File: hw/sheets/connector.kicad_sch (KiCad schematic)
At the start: 1 part, among them J1 AH58893-T9B10-3F

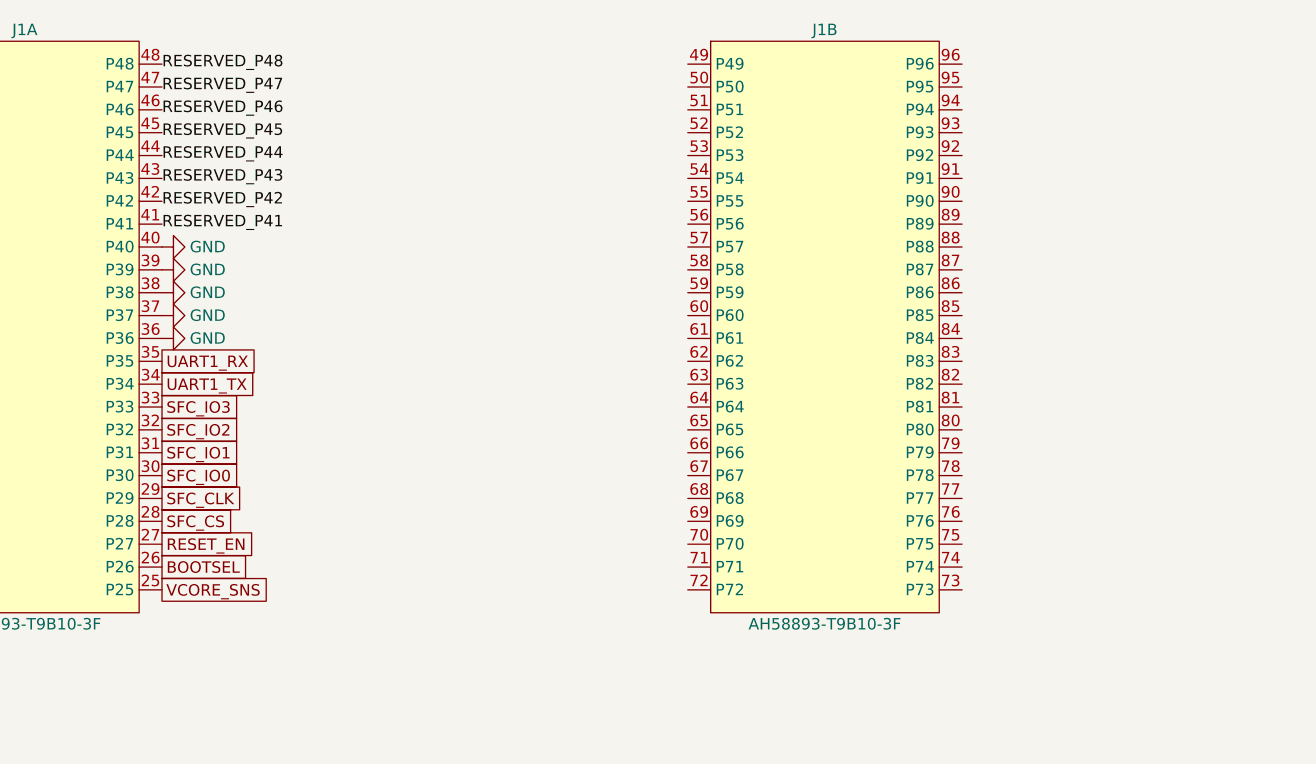
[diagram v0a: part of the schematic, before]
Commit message: Carrier board: BMC power isolation, ESP-Hosted link, GPIO expander
Rebuilds the schematic to connectivity-by-label per BUILD.md (zero
wires/junctions) across all four sections, and adds the BMC power
architecture, connector crossings, and safety fixes worked out this
session:

- Dedicated BMC USB-C (J9), isolated 5V domains (+5V_BMC/+5V_ALT/+5V_SW),
  priority DC-jack-over-USB-C P-FET OR (Q1/Q2), 2:1 load-switch select
  (U4/U14) with a genuine ON-OFF-ON manual override (SW2)
- D1/D2 diode-OR so the BMC stays powered on ALT-only input without
  reopening the J9 backfeed path
- JP1 provisioning jumper + mandatory bring-up checklist: gates SW2 until
  the digipot's NV memory has been confirmed safe, closing the
  factory-mid-scale-default overvoltage gap on VCORE
- GPIO expander (U15, TCA9555PWR) frees 9 ESP32 GPIOs for a full-duplex
  SPI link to the interposer SoC (ESP-Hosted WiFi/BLE co-processor),
  while keeping flash chip-select and power-domain switching native for
  margin testing
- microSD, headphone jack, and both MIPI camera FFCs now cross the DDR4
  connector to the interposer, with GND isolation around each block
- J2/J3 share one USB host data pair to the interposer (peripheral use,
  independent of J2's power role)
- Added missing primary SOIC-8 NOR flash chip (W25Q32JVSS) to match the
  reference board's dual-NOR layout

docs/UNIVERSAL.md updated throughout to match; CONNECTIONS.txt and the
ESP32 pinout reference regenerated from the current netlist.
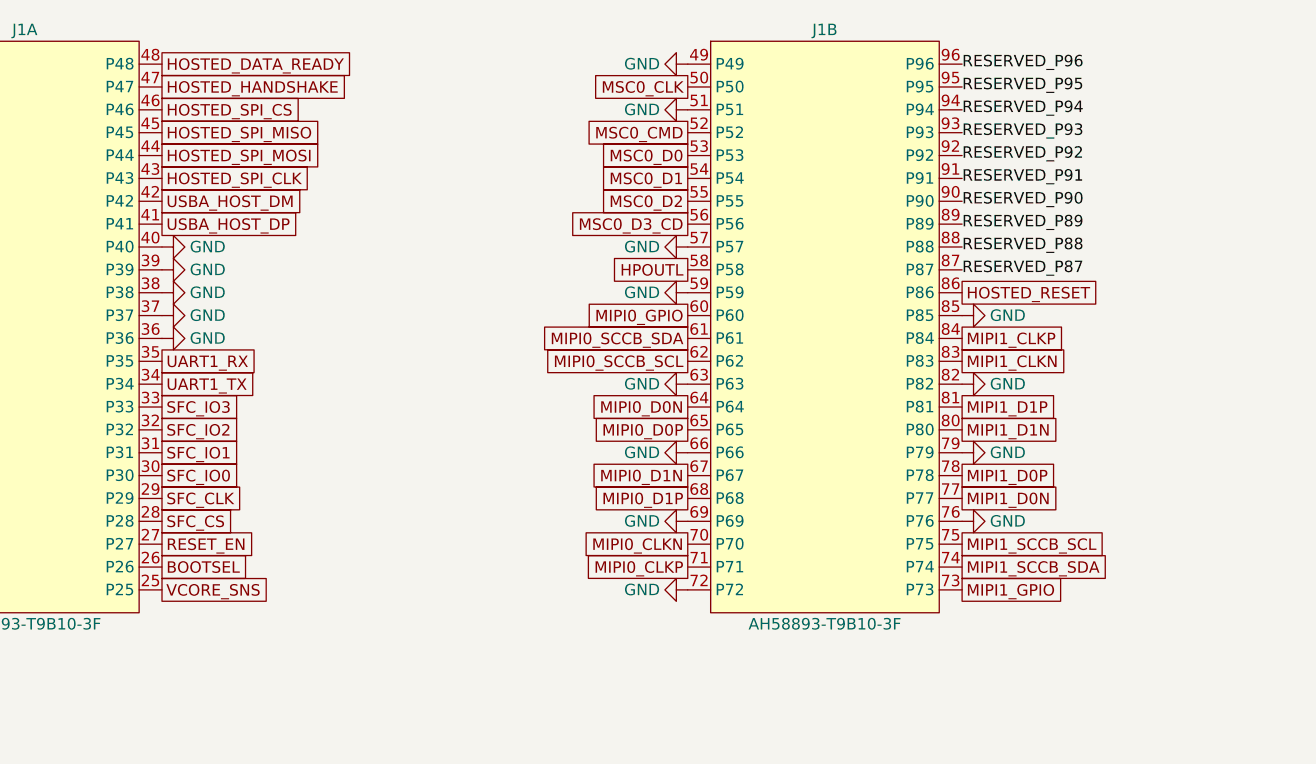
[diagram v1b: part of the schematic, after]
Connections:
- net GND: now also J1.49 (P49), J1.51 (P51), J1.57 (P57), J1.59 (P59), J1.63 (P63), J1.66 (P66), J1.69 (P69), J1.72 (P72), J1.76 (P76), J1.79 (P79), J1.82 (P82), J1.85 (P85)
- net MSC0_CLK: now reaches J1.50 (P50)
- net MSC0_CMD: now reaches J1.52 (P52)
- net MSC0_D0: now reaches J1.53 (P53)
- net MSC0_D1: now reaches J1.54 (P54)
- net MSC0_D2: now reaches J1.55 (P55)
- net MSC0_D3_CD: now reaches J1.56 (P56)
- net HPOUTL: now reaches J1.58 (P58)
- net MIPI0_GPIO: now reaches J1.60 (P60)
- net MIPI0_SCCB_SDA: now reaches J1.61 (P61)
- net MIPI0_SCCB_SCL: now reaches J1.62 (P62)
- net MIPI0_D0N: now reaches J1.64 (P64)
- net MIPI0_D0P: now reaches J1.65 (P65)
- net MIPI0_D1N: now reaches J1.67 (P67)
- net MIPI0_D1P: now reaches J1.68 (P68)
- net MIPI0_CLKN: now reaches J1.70 (P70)
- net MIPI0_CLKP: now reaches J1.71 (P71)
- net MIPI1_GPIO: now reaches J1.73 (P73)
- net MIPI1_SCCB_SDA: now reaches J1.74 (P74)
- net MIPI1_SCCB_SCL: now reaches J1.75 (P75)
- net MIPI1_D0N: now reaches J1.77 (P77)
- net MIPI1_D0P: now reaches J1.78 (P78)
- net MIPI1_D1N: now reaches J1.80 (P80)
- net MIPI1_D1P: now reaches J1.81 (P81)
- net MIPI1_CLKN: now reaches J1.83 (P83)
- net MIPI1_CLKP: now reaches J1.84 (P84)
- net HOSTED_RESET: now reaches J1.86 (P86)
- net RESERVED_P87: now reaches J1.87 (P87)
- net RESERVED_P88: now reaches J1.88 (P88)
- net RESERVED_P89: now reaches J1.89 (P89)
- net RESERVED_P90: now reaches J1.90 (P90)
- net RESERVED_P91: now reaches J1.91 (P91)
- net RESERVED_P92: now reaches J1.92 (P92)
- net RESERVED_P93: now reaches J1.93 (P93)
- net RESERVED_P94: now reaches J1.94 (P94)
- net RESERVED_P95: now reaches J1.95 (P95)
- net RESERVED_P96: now reaches J1.96 (P96)
- net RESERVED_P41 renamed USBA_HOST_DP
- net RESERVED_P42 renamed USBA_HOST_DM
- net RESERVED_P43 renamed HOSTED_SPI_CLK
- net RESERVED_P44 renamed HOSTED_SPI_MOSI
- net RESERVED_P45 renamed HOSTED_SPI_MISO
- net RESERVED_P46 renamed HOSTED_SPI_CS
- net RESERVED_P47 renamed HOSTED_HANDSHAKE
- net RESERVED_P48 renamed HOSTED_DATA_READY
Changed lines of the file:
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@@
 		(property "Value" "AH58893-T9B10-3F" (at 139.7 104.14000000000001 0) (effects (font (size 1.27 1.27))))
+	)
+	(symbol (lib_id "power:GND") (at 124.46 41.91 270) (unit 1)
+		(property "Reference" "#CGND016" (at 124.46 41.91 0) (effects (font (size 1.27 1.27)) hide))
+		(property "Value" "GND" (at 119.38 41.91 90) (effects (font (size 1.27 1.27))))
+	)
+	(symbol (lib_id "power:GND") (at 124.46 46.99 270) (unit 1)
+		(property "Reference" "#CGND017" (at 124.46 46.99 0) (effects (font (size 1.27 1.27)) hide))
+		(property "Value" "GND" (at 119.38 46.99 90) (effects (font (size 1.27 1.27))))
+	)
+	(symbol (lib_id "power:GND") (at 124.46 62.23 270) (unit 1)
+		(property "Reference" "#CGND018" (at 124.46 62.23 0) (effects (font (size 1.27 1.27)) hide))
+		(property "Value" "GND" (at 119.38 62.23 90) (effects (font (size 1.27 1.27))))
+	)
+	(symbol (lib_id "power:GND") (at 124.46 67.31 270) (unit 1)
+		(property "Reference" "#CGND019" (at 124.46 67.31 0) (effects (font (size 1.27 1.27)) hide))
+		(property "Value" "GND" (at 119.38 67.31 90) (effects (font (size 1.27 1.27))))
+	)
+	(symbol (lib_id "power:GND") (at 124.46 77.47 270) (unit 1)
+		(property "Reference" "#CGND020" (at 124.46 77.47 0) (effects (font (size 1.27 1.27)) hide))
+		(property "Value" "GND" (at 119.38 77.47 90) (effects (font (size 1.27 1.27))))
+	)
+	(symbol (lib_id "power:GND") (at 124.46 85.09 270) (unit 1)
+		(property "Reference" "#CGND021" (at 124.46 85.09 0) (effects (font (size 1.27 1.27)) hide))
+		(property "Value" "GND" (at 119.38 85.09 90) (effects (font (size 1.27 1.27))))
+	)
+	(symbol (lib_id "power:GND") (at 124.46 92.71 270) (unit 1)
+		(property "Reference" "#CGND022" (at 124.46 92.71 0) (effects (font (size 1.27 1.27)) hide))
+		(property "Value" "GND" (at 119.38 92.71 90) (effects (font (size 1.27 1.27))))
+	)
+	(symbol (lib_id "power:GND") (at 124.46 100.33 270) (unit 1)
+		(property "Reference" "#CGND023" (at 124.46 100.33 0) (effects (font (size 1.27 1.27)) hide))
+		(property "Value" "GND" (at 119.38 100.33 90) (effects (font (size 1.27 1.27))))
+	)
+	(symbol (lib_id "power:GND") (at 154.94 92.71 90) (unit 1)
+		(property "Reference" "#CGND024" (at 154.94 92.71 0) (effects (font (size 1.27 1.27)) hide))
+		(property "Value" "GND" (at 160.02 92.71 270) (effects (font (size 1.27 1.27))))
+	)
+	(symbol (lib_id "power:GND") (at 154.94 85.09 90) (unit 1)
+		(property "Reference" "#CGND025" (at 154.94 85.09 0) (effects (font (size 1.27 1.27)) hide))
+		(property "Value" "GND" (at 160.02 85.09 270) (effects (font (size 1.27 1.27))))
+	)
+	(symbol (lib_id "power:GND") (at 154.94 77.47 90) (unit 1)
+		(property "Reference" "#CGND026" (at 154.94 77.47 0) (effects (font (size 1.27 1.27)) hide))
+		(property "Value" "GND" (at 160.02 77.47 270) (effects (font (size 1.27 1.27))))
+	)
+	(symbol (lib_id "power:GND") (at 154.94 69.85 90) (unit 1)
+		(property "Reference" "#CGND027" (at 154.94 69.85 0) (effects (font (size 1.27 1.27)) hide))
+		(property "Value" "GND" (at 160.02 69.85 270) (effects (font (size 1.27 1.27))))
 	)
 	(symbol (lib_id "teacup-carrier:AH58893-T9B10-3F") (at 228.6 71.12 0) (unit 3)
@@
 	(global_label "UART1_TX" (at 66.04 77.47 0) (effects (font (size 1.27 1.27)) (justify left)))
 	(global_label "UART1_RX" (at 66.04 74.93 0) (effects (font (size 1.27 1.27)) (justify left)))
-	(label "RESERVED_P41" (at 66.04 59.69 0) (effects (font (size 1.27 1.27)) (justify left)))
-	(label "RESERVED_P42" (at 66.04 57.15 0) (effects (font (size 1.27 1.27)) (justify left)))
-	(label "RESERVED_P43" (at 66.04 54.61 0) (effects (font (size 1.27 1.27)) (justify left)))
-	(label "RESERVED_P44" (at 66.04 52.07 0) (effects (font (size 1.27 1.27)) (justify left)))
-	(label "RESERVED_P45" (at 66.04 49.53 0) (effects (font (size 1.27 1.27)) (justify left)))
-	(label "RESERVED_P46" (at 66.04 46.99 0) (effects (font (size 1.27 1.27)) (justify left)))
-	(label "RESERVED_P47" (at 66.04 44.45 0) (effects (font (size 1.27 1.27)) (justify left)))
-	(label "RESERVED_P48" (at 66.04 41.91 0) (effects (font (size 1.27 1.27)) (justify left)))
+	(global_label "USBA_HOST_DP" (at 66.04 59.69 0) (effects (font (size 1.27 1.27)) (justify left)))
+	(global_label "USBA_HOST_DM" (at 66.04 57.15 0) (effects (font (size 1.27 1.27)) (justify left)))
+	(global_label "HOSTED_SPI_CLK" (at 66.04 54.61 0) (effects (font (size 1.27 1.27)) (justify left)))
+	(global_label "HOSTED_SPI_MOSI" (at 66.04 52.07 0) (effects (font (size 1.27 1.27)) (justify left)))
+	(global_label "HOSTED_SPI_MISO" (at 66.04 49.53 0) (effects (font (size 1.27 1.27)) (justify left)))
+	(global_label "HOSTED_SPI_CS" (at 66.04 46.99 0) (effects (font (size 1.27 1.27)) (justify left)))
+	(global_label "HOSTED_HANDSHAKE" (at 66.04 44.45 0) (effects (font (size 1.27 1.27)) (justify left)))
+	(global_label "HOSTED_DATA_READY" (at 66.04 41.91 0) (effects (font (size 1.27 1.27)) (justify left)))
+	(global_label "MSC0_CLK" (at 124.46 44.45 180) (effects (font (size 1.27 1.27)) (justify right)))
+	(global_label "MSC0_CMD" (at 124.46 49.53 180) (effects (font (size 1.27 1.27)) (justify right)))
+	(global_label "MSC0_D0" (at 124.46 52.07 180) (effects (font (size 1.27 1.27)) (justify right)))
+	(global_label "MSC0_D1" (at 124.46 54.61 180) (effects (font (size 1.27 1.27)) (justify right)))
+	(global_label "MSC0_D2" (at 124.46 57.15 180) (effects (font (size 1.27 1.27)) (justify right)))
+	(global_label "MSC0_D3_CD" (at 124.46 59.69 180) (effects (font (size 1.27 1.27)) (justify right)))
+	(global_label "HPOUTL" (at 124.46 64.77 180) (effects (font (size 1.27 1.27)) (justify right)))
+	(global_label "MIPI0_GPIO" (at 124.46 69.85 180) (effects (font (size 1.27 1.27)) (justify right)))
+	(global_label "MIPI0_SCCB_SDA" (at 124.46 72.39 180) (effects (font (size 1.27 1.27)) (justify right)))
+	(global_label "MIPI0_SCCB_SCL" (at 124.46 74.93 180) (effects (font (size 1.27 1.27)) (justify right)))
+	(global_label "MIPI0_D0N" (at 124.46 80.01 180) (effects (font (size 1.27 1.27)) (justify right)))
+	(global_label "MIPI0_D0P" (at 124.46 82.55 180) (effects (font (size 1.27 1.27)) (justify right)))
+	(global_label "MIPI0_D1N" (at 124.46 87.63 180) (effects (font (size 1.27 1.27)) (justify right)))
+	(global_label "MIPI0_D1P" (at 124.46 90.17 180) (effects (font (size 1.27 1.27)) (justify right)))
+	(global_label "MIPI0_CLKN" (at 124.46 95.25 180) (effects (font (size 1.27 1.27)) (justify right)))
+	(global_label "MIPI0_CLKP" (at 124.46 97.79 180) (effects (font (size 1.27 1.27)) (justify right)))
+	(global_label "MIPI1_GPIO" (at 154.94 100.33 0) (effects (font (size 1.27 1.27)) (justify left)))
+	(global_label "MIPI1_SCCB_SDA" (at 154.94 97.79 0) (effects (font (size 1.27 1.27)) (justify left)))
+	(global_label "MIPI1_SCCB_SCL" (at 154.94 95.25 0) (effects (font (size 1.27 1.27)) (justify left)))
+	(global_label "MIPI1_D0N" (at 154.94 90.17 0) (effects (font (size 1.27 1.27)) (justify left)))
+	(global_label "MIPI1_D0P" (at 154.94 87.63 0) (effects (font (size 1.27 1.27)) (justify left)))
+	(global_label "MIPI1_D1N" (at 154.94 82.55 0) (effects (font (size 1.27 1.27)) (justify left)))
+	(global_label "MIPI1_D1P" (at 154.94 80.01 0) (effects (font (size 1.27 1.27)) (justify left)))
+	(global_label "MIPI1_CLKN" (at 154.94 74.93 0) (effects (font (size 1.27 1.27)) (justify left)))
+	(global_label "MIPI1_CLKP" (at 154.94 72.39 0) (effects (font (size 1.27 1.27)) (justify left)))
+	(global_label "HOSTED_RESET" (at 154.94 67.31 0) (effects (font (size 1.27 1.27)) (justify left)))
+	(label "RESERVED_P87" (at 154.94 64.77 0) (effects (font (size 1.27 1.27)) (justify left)))
+	(label "RESERVED_P88" (at 154.94 62.23 0) (effects (font (size 1.27 1.27)) (justify left)))
+	(label "RESERVED_P89" (at 154.94 59.69 0) (effects (font (size 1.27 1.27)) (justify left)))
+	(label "RESERVED_P90" (at 154.94 57.15 0) (effects (font (size 1.27 1.27)) (justify left)))
+	(label "RESERVED_P91" (at 154.94 54.61 0) (effects (font (size 1.27 1.27)) (justify left)))
+	(label "RESERVED_P92" (at 154.94 52.07 0) (effects (font (size 1.27 1.27)) (justify left)))
+	(label "RESERVED_P93" (at 154.94 49.53 0) (effects (font (size 1.27 1.27)) (justify left)))
+	(label "RESERVED_P94" (at 154.94 46.99 0) (effects (font (size 1.27 1.27)) (justify left)))
+	(label "RESERVED_P95" (at 154.94 44.45 0) (effects (font (size 1.27 1.27)) (justify left)))
+	(label "RESERVED_P96" (at 154.94 41.91 0) (effects (font (size 1.27 1.27)) (justify left)))
 	(sheet_instances
 		(path "/016abe51-c097-4611-854e-0af763646499"
